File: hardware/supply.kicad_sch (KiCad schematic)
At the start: 31 parts

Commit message: Fixed Logic
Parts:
- added U?: 4011, symbol 4xxx:4011
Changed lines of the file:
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@@
   (junction (at 172.72 119.38) (diameter 0) (color 0 0 0 0)
   )
+  (junction (at 250.19 80.01) (diameter 0) (color 0 0 0 0)
+  )
   (junction (at 254 119.38) (diameter 0) (color 0 0 0 0)
   )
@@
     (stroke (width 0) (type default) (color 0 0 0 0))
   )
+  (wire (pts (xy 250.19 80.01) (xy 254 80.01))
+    (stroke (width 0) (type default) (color 0 0 0 0))
+  )
   (wire (pts (xy 120.65 83.82) (xy 143.51 83.82))
     (stroke (width 0) (type default) (color 0 0 0 0))
@@
     (stroke (width 0) (type default) (color 0 0 0 0))
   )
-  (wire (pts (xy 242.57 80.01) (xy 254 80.01))
+  (wire (pts (xy 242.57 80.01) (xy 250.19 80.01))
     (stroke (width 0) (type default) (color 0 0 0 0))
   )
@@
     (pin "1")
   )
+  (symbol (lib_id "4xxx:4011") (at 100.33 170.18 0) (unit 5)
+    (in_bom yes) (on_board yes) (fields_autoplaced)
+    (property "Reference" "U?" (id 0) (at 106.68 168.9099 0)
+      (effects (font (size 1.27 1.27)) (justify left))
+    )
+    (property "Value" "4011" (id 1) (at 106.68 171.4499 0)
+      (effects (font (size 1.27 1.27)) (justify left))
+    )
+    (property "Footprint" "" (id 2) (at 100.33 170.18 0)
+      (effects (font (size 1.27 1.27)) hide)
+    )
+    (property "Datasheet" "http://www.intersil.com/content/dam/Intersil/documents/cd40/cd4011bms-12bms-23bms.pdf" (id 3) (at 100.33 170.18 0)
+      (effects (font (size 1.27 1.27)) hide)
+    )
+    (pin "1")
+    (pin "2")
+    (pin "3")
+    (pin "4")
+    (pin "5")
+    (pin "6")
+    (pin "10")
+    (pin "8")
+    (pin "9")
+    (pin "11")
+    (pin "12")
+    (pin "13")
+    (pin "14")
+    (pin "7")
+  )
   (symbol (lib_id "Device:LED") (at 201.93 92.71 90) (unit 1)
     (in_bom yes) (on_board yes)
@@
       (effects (font (size 1.27 1.27)) hide)
     )
+    (pin "1")
+  )
+  (symbol (lib_id "power:PWR_FLAG") (at 250.19 80.01 0) (unit 1)
+    (in_bom yes) (on_board yes) (fields_autoplaced)
+    (property "Reference" "#FLG?" (id 0) (at 250.19 78.105 0)
+      (effects (font (size 1.27 1.27)) hide)
+    )
+    (property "Value" "PWR_FLAG" (id 1) (at 250.19 74.93 0))
+    (property "Footprint" "" (id 2) (at 250.19 80.01 0)
+      (effects (font (size 1.27 1.27)) hide)
+    )
+    (property "Datasheet" "~" (id 3) (at 250.19 80.01 0)
+      (effects (font (size 1.27 1.27)) hide)
+    )

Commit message: Alpha 1.0.0 Schematic
First Schematic Version for initial checkup
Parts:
- D?: value SMBJ18CA-E3/52 -> SD24-SOD323
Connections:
- net VCC is gone; now on net +3V3: C?.1, D?.1 (K), U?.14 (VDD), U?.14 (VDD)
- net +3V3: now also U?.14 (VDD)
- net GND: now also U?.7 (VSS)
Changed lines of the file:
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@@
   (junction (at 105.41 119.38) (diameter 0) (color 0 0 0 0)
   )
+  (junction (at 115.57 182.88) (diameter 0) (color 0 0 0 0)
+  )
   (junction (at 77.47 80.01) (diameter 0) (color 0 0 0 0)
   )
@@
   (junction (at 214.63 119.38) (diameter 0) (color 0 0 0 0)
   )
+  (junction (at 115.57 156.21) (diameter 0) (color 0 0 0 0)
+  )
   (junction (at 265.43 80.01) (diameter 0) (color 0 0 0 0)
   )
@@
     (stroke (width 0) (type default) (color 0 0 0 0))
   )
+  (wire (pts (xy 100.33 156.21) (xy 115.57 156.21))
+    (stroke (width 0) (type default) (color 0 0 0 0))
+  )
   (wire (pts (xy 144.78 80.01) (xy 172.72 80.01))
     (stroke (width 0) (type default) (color 0 0 0 0))
@@
     (stroke (width 0) (type default) (color 0 0 0 0))
   )
+  (wire (pts (xy 100.33 157.48) (xy 100.33 156.21))
+    (stroke (width 0) (type default) (color 0 0 0 0))
+  )
   (wire (pts (xy 124.46 77.47) (xy 124.46 80.01))
     (stroke (width 0) (type default) (color 0 0 0 0))
@@
   )
   (wire (pts (xy 228.6 87.63) (xy 228.6 119.38))
+    (stroke (width 0) (type default) (color 0 0 0 0))
+  )
+  (wire (pts (xy 100.33 182.88) (xy 115.57 182.88))
     (stroke (width 0) (type default) (color 0 0 0 0))
   )
@@
   )
   (symbol (lib_id "Device:C") (at 71.12 87.63 0) (unit 1)
-    (in_bom yes) (on_board yes) (fields_autoplaced)
-    (property "Reference" "C?" (id 0) (at 74.93 86.3599 0)
-      (effects (font (size 1.27 1.27)) (justify left))
-    )
-    (property "Value" "10uF low ESR" (id 1) (at 74.93 88.8999 0)
+    (in_bom yes) (on_board yes)
+    (property "Reference" "C?" (id 0) (at 73.66 86.36 0)
+      (effects (font (size 1.27 1.27)) (justify left))
+    )
+    (property "Value" "10uF low ESR" (id 1) (at 73.66 88.9 0)
       (effects (font (size 1.27 1.27)) (justify left))
     )
@@
     (pin "2")
   )
-  (symbol (lib_id "power:VCC") (at 142.24 153.67 0) (unit 1)
+  (symbol (lib_id "power:+3V3") (at 142.24 153.67 0) (unit 1)
     (in_bom yes) (on_board yes) (fields_autoplaced)
     (property "Reference" "#PWR?" (id 0) (at 142.24 157.48 0)
       (effects (font (size 1.27 1.27)) hide)
     )
-    (property "Value" "VCC" (id 1) (at 142.24 148.59 0))
+    (property "Value" "+3V3" (id 1) (at 142.24 148.59 0))
     (property "Footprint" "" (id 2) (at 142.24 153.67 0)
       (effects (font (size 1.27 1.27)) hide)
@@
       (effects (font (size 1.27 1.27)) (justify left))
     )
-    (property "Value" "SMBJ18CA-E3/52" (id 1) (at 39.37 88.9 90)
+    (property "Value" "SD24-SOD323" (id 1) (at 39.37 88.9 90)
       (effects (font (size 1.27 1.27)) (justify left))
     )
@@
   )
   (symbol (lib_id "Device:C") (at 60.96 87.63 0) (unit 1)
-    (in_bom yes) (on_board yes) (fields_autoplaced)
-    (property "Reference" "C?" (id 0) (at 64.77 86.3599 0)
-      (effects (font (size 1.27 1.27)) (justify left))
-    )
-    (property "Value" "47uF" (id 1) (at 64.77 88.8999 0)
-      (effects (font (size 1.27 1.27)) (justify left))
-    )
+    (in_bom yes) (on_board yes)
+    (property "Reference" "C?" (id 0) (at 63.5 86.36 0)
+      (effects (font (size 1.27 1.27)) (justify left))
+    )
+    (property "Value" "47uF" (id 1) (at 63.5 88.9 0)
+      (effects (font (size 1.27 1.27)) (justify left))
+    )

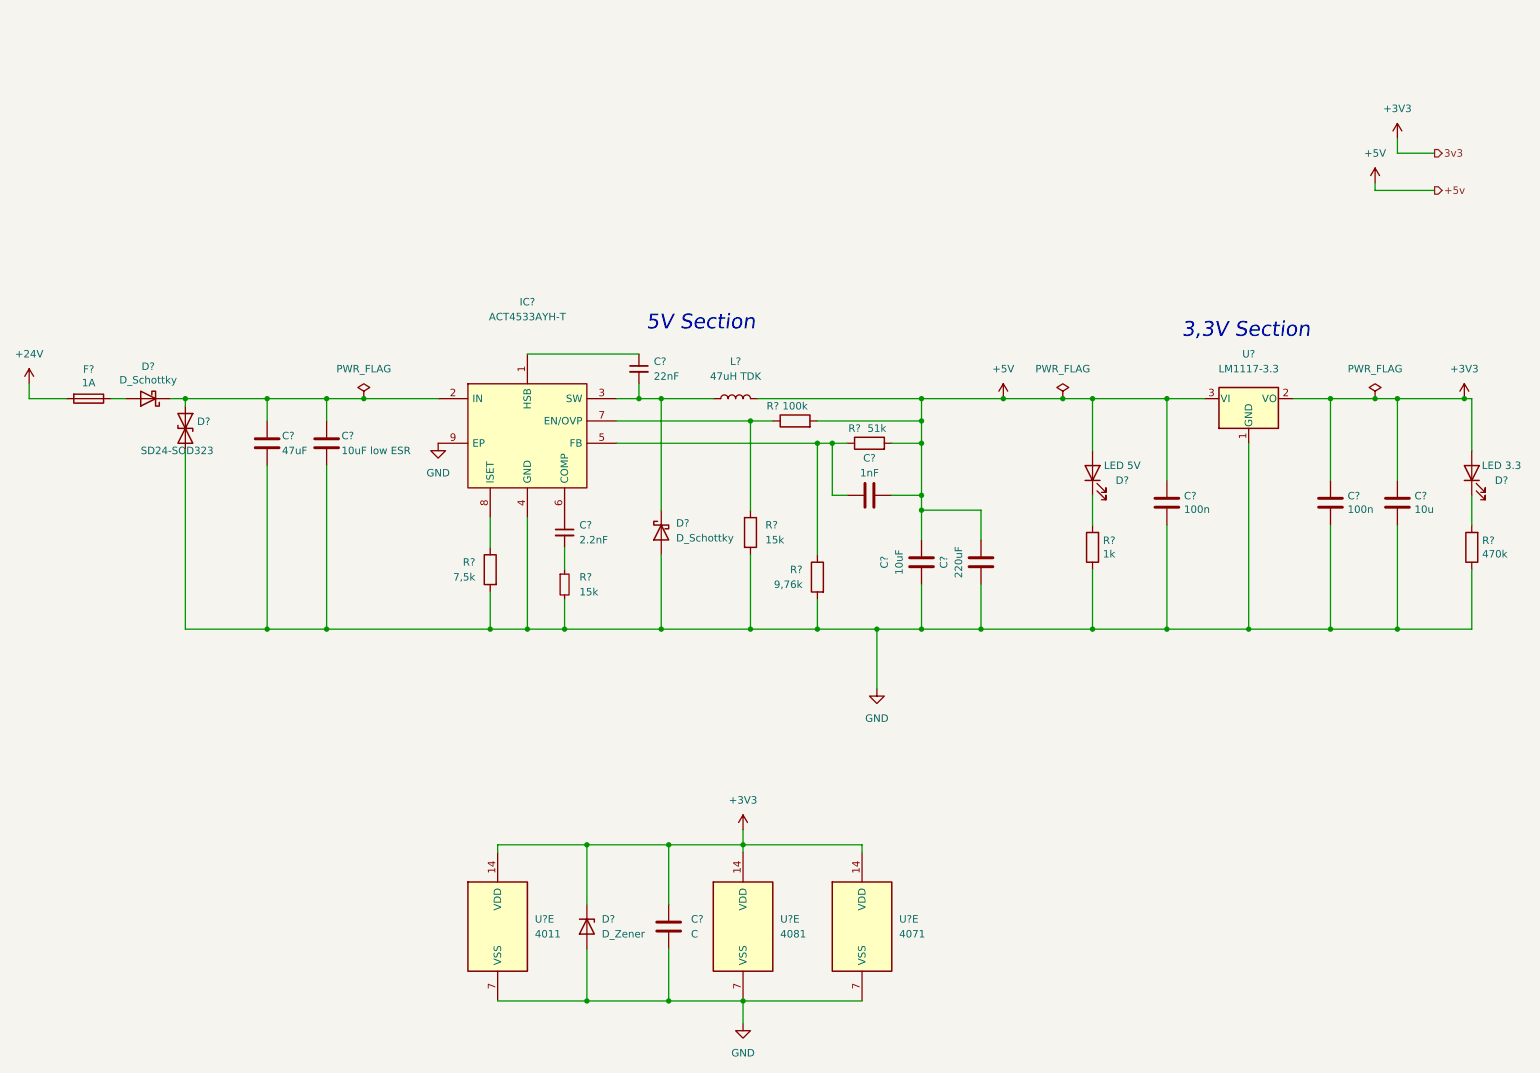
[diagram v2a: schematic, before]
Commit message: Minor changes on v1 schematic
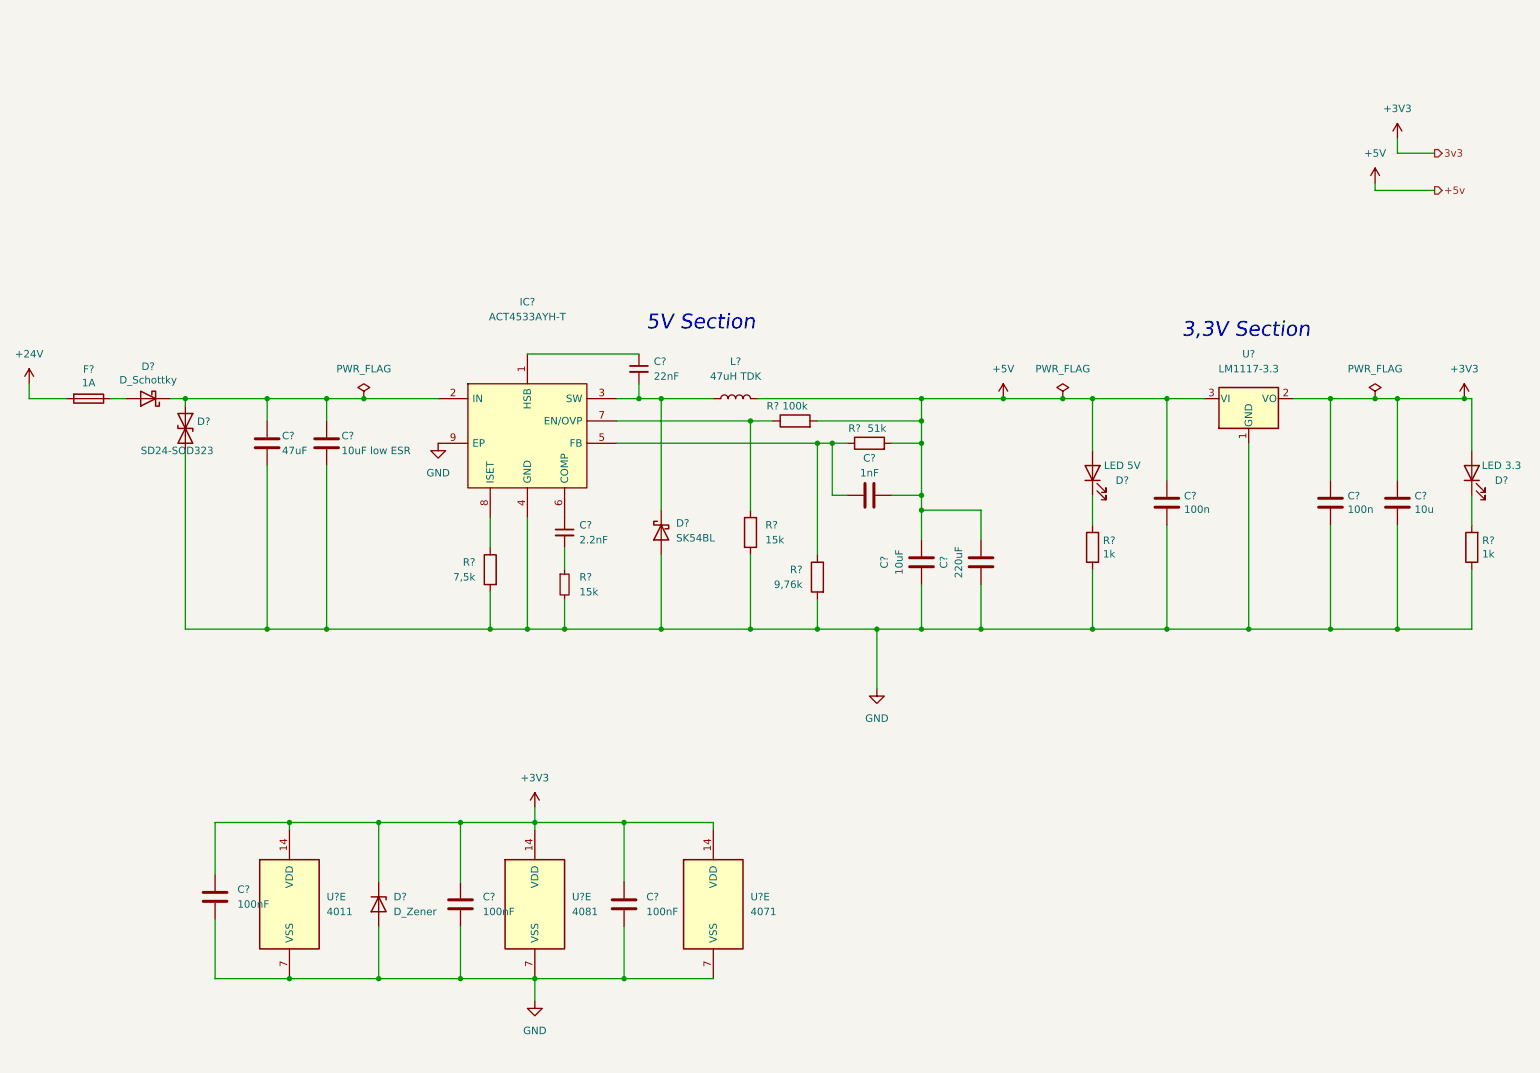
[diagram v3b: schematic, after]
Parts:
- added C? (x2): 100nF, symbol Device:C
- C?: value C -> 100nF
- D?: value D_Schottky -> SK54BL
- R?: value 470k -> 1k
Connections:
- net +3V3: now also C?.1, C?.1
- net GND: now also C?.2, C?.2
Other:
- moved on the sheet: C?, D?, U?E

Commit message: minor schematic cleanup
Fixes before second review
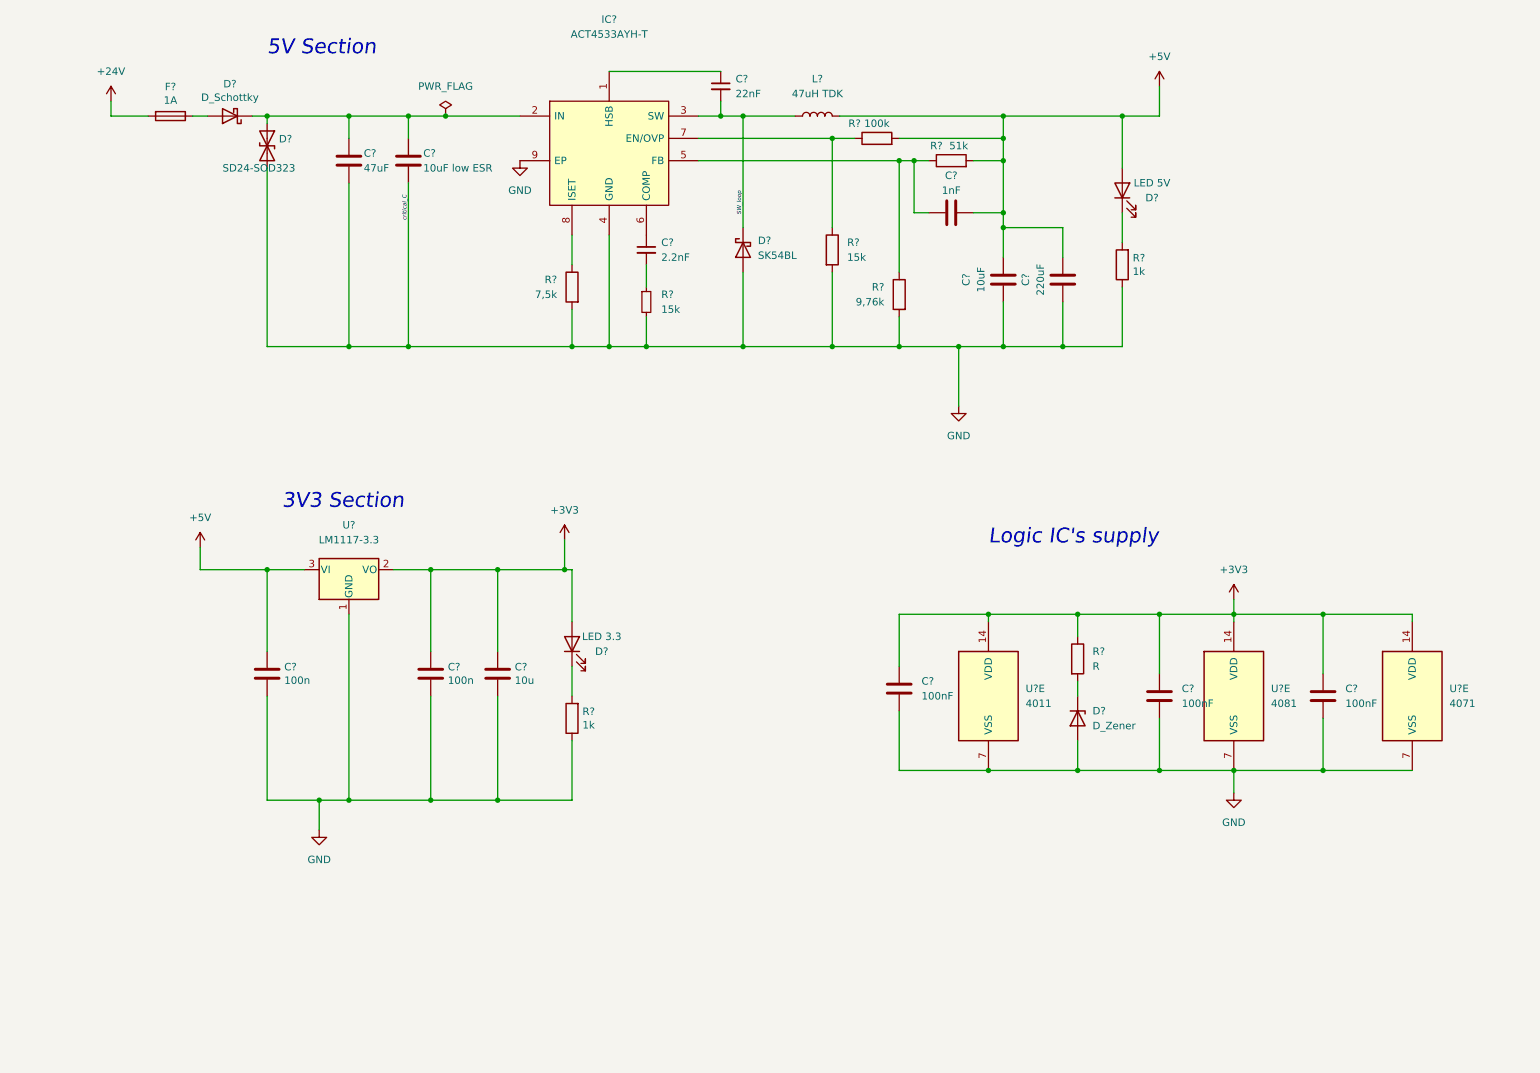
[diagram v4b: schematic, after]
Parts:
- added R?: R, symbol Device:R
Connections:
- net +3V3: now also R?.1; no longer D?.1 (K)
- net SW_loop: now reaches C?.2, D?.1 (K), IC?.3 (SW), L?.1
- new net: D?.1 (K), R?.2
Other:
- note added: "3V3 Section"
- note added: "Logic IC's supply"
- note removed: "3,3V Section"
- company: (none) -> PUT Motorsport
- title: (none) -> Power supply section
- moved on the sheet: C?, D?, F?, IC?, L?, R?, U?, U?E

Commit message: Schematic ready for second review
Cleaned up, numerated, added footprints, JW notes considered
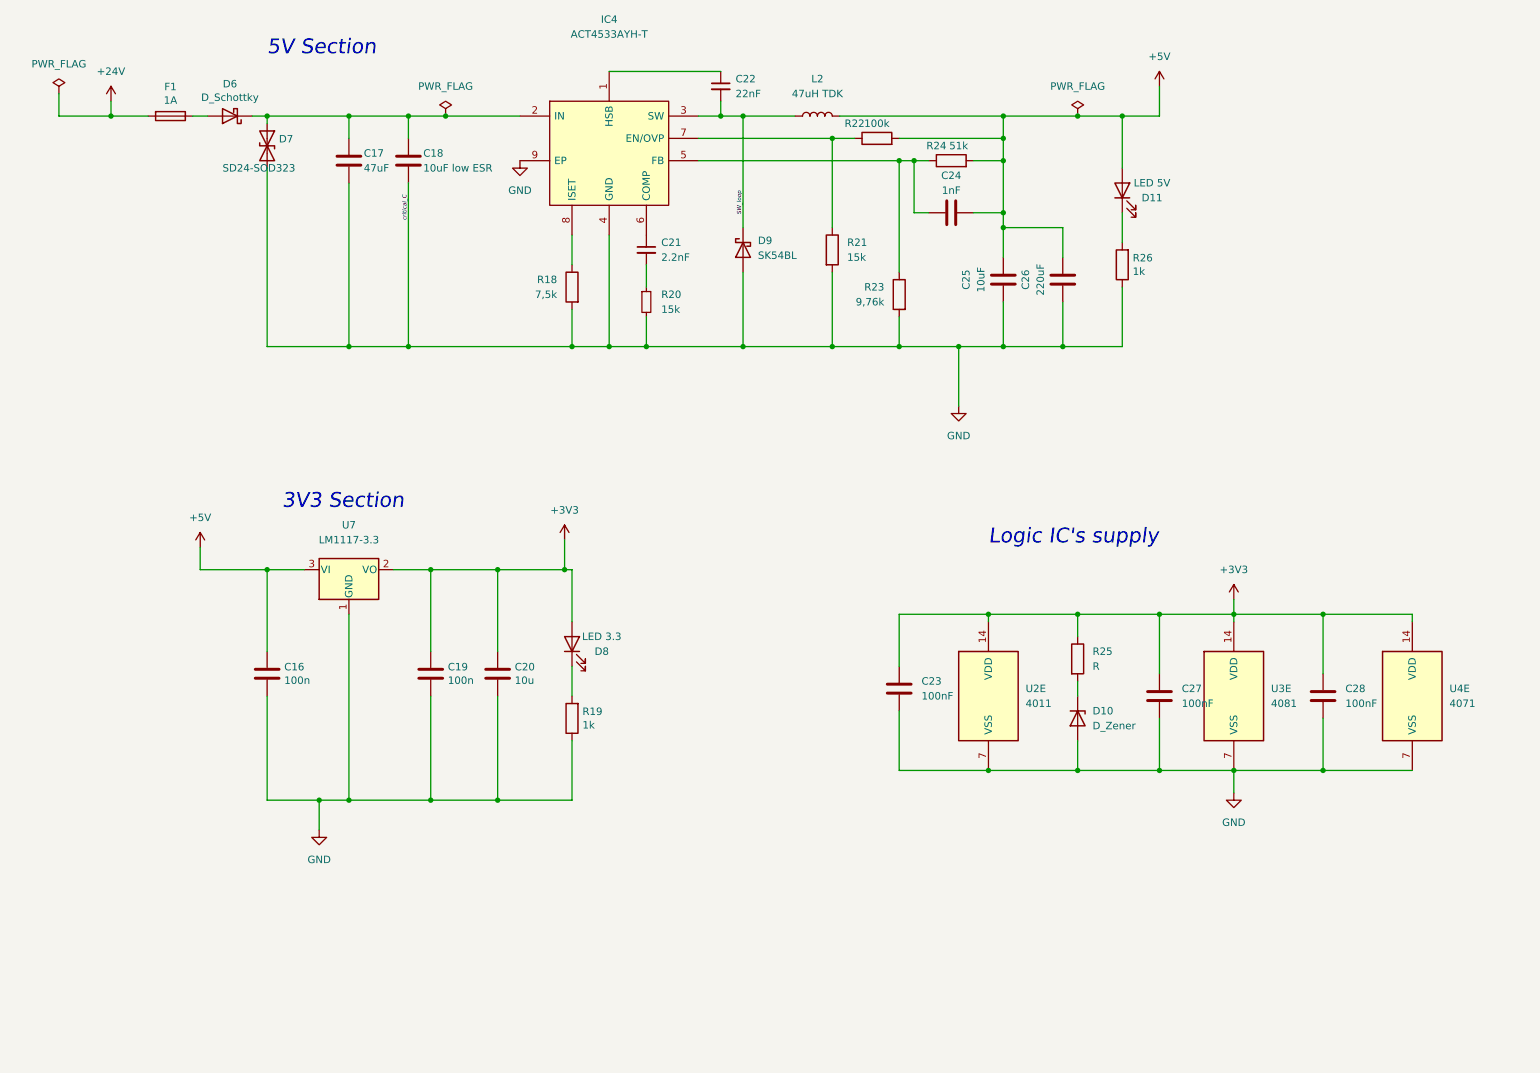
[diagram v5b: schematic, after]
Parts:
- C23, C27, C28: renamed from C?; footprint (none) -> Capacitor_SMD:C_0201_0603Metric_Pad0.64x0.40mm_HandSolder
- D10: renamed from D?; footprint (none) -> Diode_SMD:D_SMB
- R25: renamed from R?; footprint (none) -> Resistor_SMD:R_0603_1608Metric
- gave numbers to parts that had none: 30
